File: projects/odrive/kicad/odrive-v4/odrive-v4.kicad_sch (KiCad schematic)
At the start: 0 parts

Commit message: Build the ODrive v3.5 and v4 schematics, both verified
The v3.5 recreation (Top + MotorCell M0/M1 + AuxHalfH) matches the netlist
ground truth extracted from the Altium PDF's embedded text layer — every
component, value and net membership diffed clean, ERC 0 errors. The v4
schematic implements docs/v4-design.md across 10 block sheets, 375 parts,
ERC 0 errors, with the STM32 pin map verified pin-by-pin against v3.5;
only the design doc's declared changes differ (PA2/PA3 SO3 jumpers,
PB2/PB10 mux selects, PC4 mux common).

Both were built through Konnect MCP tools by the e2e workflow's oracle
loops; the v4 ERC count converged 740 -> 579 -> 144 -> 2 -> 0 across five
fix rounds. The project sym-lib-tables pin absolute /nix/store paths and
need re-registering if the kicad pin moves; the schematics embed their
symbols, so they open regardless. Details in docs/LOG.md; layout and fab
outputs are the remaining phases.
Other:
- added sheet Brake Chopper (brake.kicad_sch)
- added sheet CAN (can.kicad_sch)
- added sheet Encoders & GPIO (encoders-gpio.kicad_sch)
- added sheet MCU (mcu.kicad_sch)
- added sheet MotorCell M0 (motorcell-m0.kicad_sch)
- added sheet MotorCell M1 (motorcell-m1.kicad_sch)
- added sheet Power Input & Protection (power-input-protection.kicad_sch)
- added sheet Rails (rails.kicad_sch)
- added sheet Sensing (sensing.kicad_sch)
- added sheet USB (usb.kicad_sch)

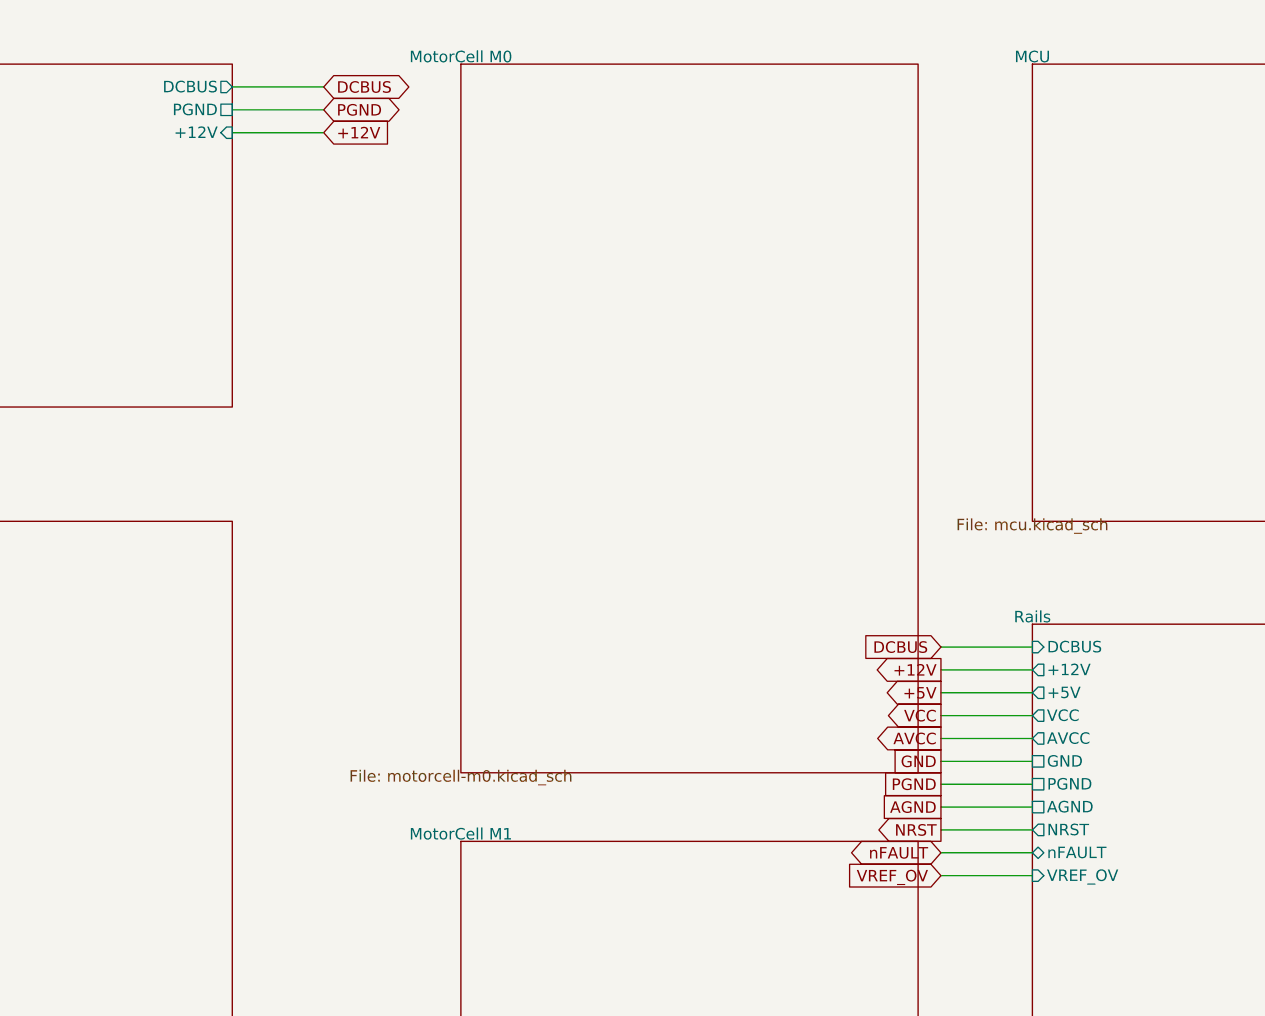
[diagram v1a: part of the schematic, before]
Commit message: Even out the bulk bank pitch, and add M3 mounting holes to the schematic
The bank was on one line but not evenly spaced - the gaps ran 16, 11.5, 12,
12, 12, 12, 15.5 mm, because the earlier pass snapped Y to a row and kept
whatever X the shelf packer had left. Visibly uneven once you zoom in. Now a
uniform 13 mm pitch from 87 to 178, which leaves 3 mm of air between the 10 mm
bodies. Verdict stays pass with no hard failures.

Also keeps H1-H4: plated M3 mounting holes belong in the schematic so the pads
land on GND in the netlist rather than showing up as stray copper. ERC is still
clean at 0 violations. They are not pushed to the board yet - that needs an
update_pcb_from_schematic run.
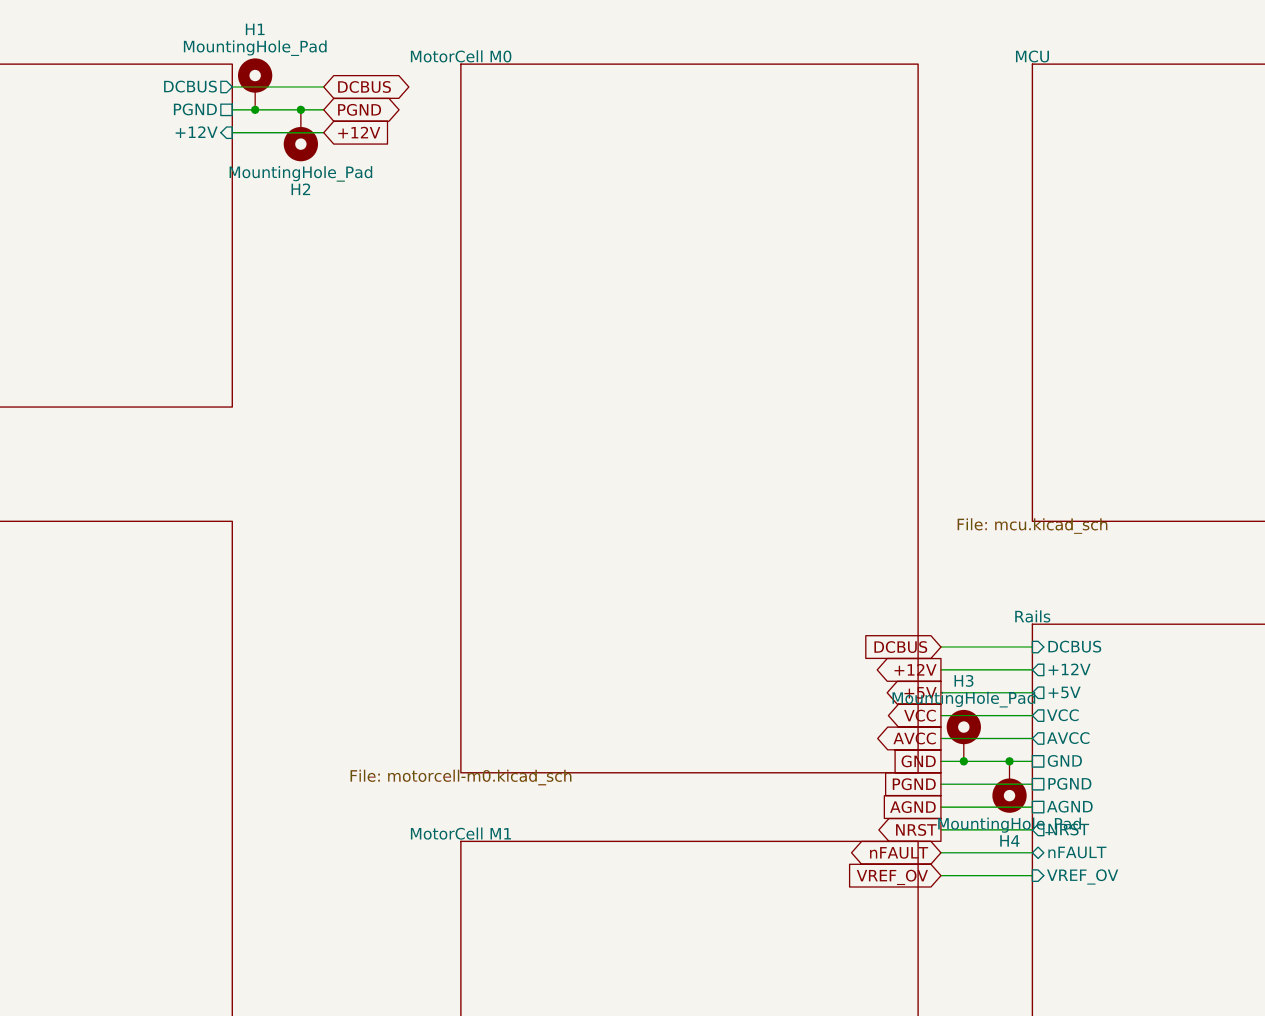
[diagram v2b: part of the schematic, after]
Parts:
- added H1, H2, H3, H4: MountingHole_Pad, symbol Mechanical:MountingHole_Pad
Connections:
- net GND: now also H3.1, H4.1
- net PGND: now also H1.1, H2.1
